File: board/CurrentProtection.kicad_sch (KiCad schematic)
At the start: 0 parts

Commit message: Schematics without values
Votlage Sensing circuit schematic
Oring controller circuit schematic
No values for components yet
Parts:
- added BT1, BT2: Battery, symbol Device:Battery
- added C1, C2, C3, C4, C5: C, symbol Device:C
- added D1, D2, D3, D4, D5: SS16, Diode_SMD:D_SMA, symbol Diode:SS16
- added D6: LED, symbol Device:LED
- added Q1, Q2, Q3: DMN3008SFG, Package_SON:Diodes_PowerDI3333-8, symbol Transistor_FET:DMN3008SFG
- added R1, R2, R27: R_US, symbol Device:R_US
- added U1, U2, U3: LM5050MK-1_NOPB, LM5050MK-1_NOPB:SOT95P280X110-6N, symbol LM5050MK-1_NOPB:LM5050MK-1_NOPB
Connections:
- new net: BT2.1 (+), D5.1 (K), Q3.1 (S), Q3.2 (S), Q3.3 (S), U3.4 (IN)
- new net: C2.1, R1.2, U1.1 (VS)
- new net: Q1.4 (G), U1.5 (GATE)
- new net: D6.2 (A), R27.2
- new net: BT1.1 (+), D4.1 (K), Q2.1 (S), Q2.2 (S), Q2.3 (S), U2.4 (IN)
- new net: Q2.4 (G), U2.5 (GATE)
- new net: Q3.4 (G), U3.5 (GATE)
- new net: D1.2 (A), D2.2 (A)
- new net +24V: C1.1, D1.1 (K), Q1.1 (S), Q1.2 (S), Q1.3 (S), U1.4 (IN)
- new net GND: BT1.2 (-), BT2.2 (-), C1.2, C2.2, C3.2, C4.2, C5.2, D2.1 (K), D3.2 (A), D4.2 (A), D5.2 (A), D6.1 (K), R2.2, U1.2 (GND), U1.3 (OFF), U2.2 (GND), U3.2 (GND)
- new net Vout: C3.1, C4.1, C5.1, D3.1 (K), Q1.5 (D), Q2.5 (D), Q3.5 (D), R1.1, R2.1, U1.6 (OUT), U2.1 (VS), U2.6 (OUT), U3.1 (VS), U3.6 (OUT)
- new net VoutPin: R27.1
- no-connect marks 0 -> 2
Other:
- note added: "LED CIRCUITS"

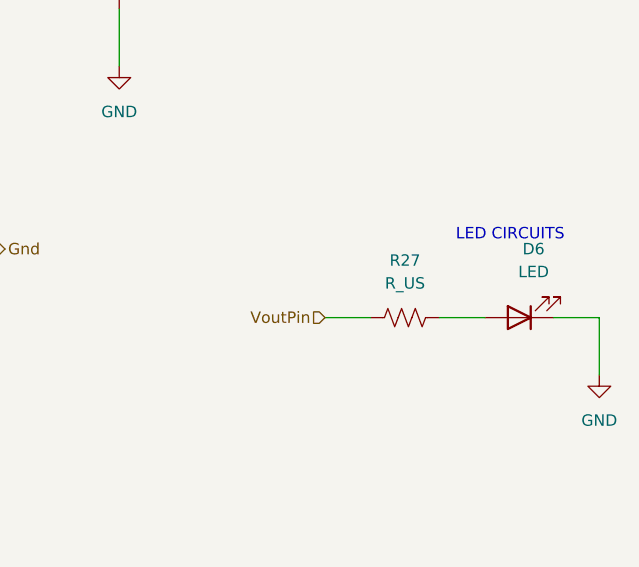
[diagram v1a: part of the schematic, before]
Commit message: Resistor Values
Added resistor values for everything on voltage sensing circuit
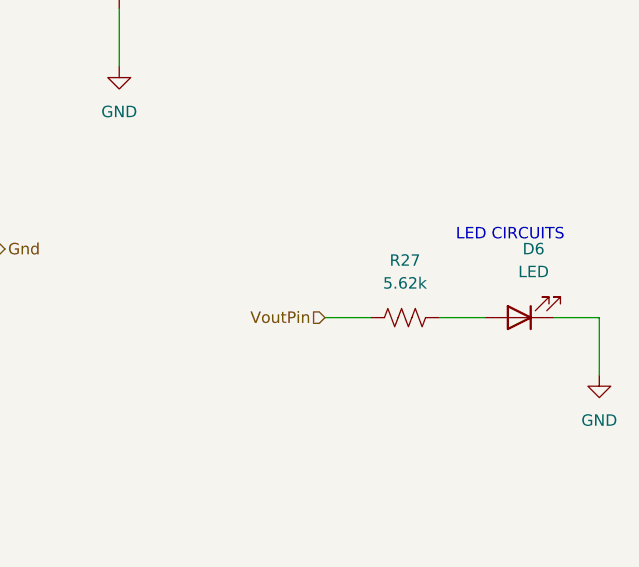
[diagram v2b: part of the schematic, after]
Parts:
- R27: value R_US -> 5.62k
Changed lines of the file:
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@@
 			)
 		)
-		(property "Value" "R_US"
+		(property "Value" "5.62k"
 			(at 176.53 138.43 90)
 			(effects

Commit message: Changed Flags
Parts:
- removed C1, C2, C3: C, symbol Device:C
- removed D1, D2, D3: SS16, Diode_SMD:D_SMA, symbol Diode:SS16
- removed Q1, Q2: DMN3008SFG, Package_SON:Diodes_PowerDI3333-8, symbol Transistor_FET:DMN3008SFG
- removed R1: R_US, symbol Device:R_US
- removed U1: LM5050MK-1_NOPB, LM5050MK-1_NOPB:SOT95P280X110-6N, symbol LM5050MK-1_NOPB:LM5050MK-1_NOPB
- added Q4: IPB180N10S4-02, Package_TO_SOT_SMD:TO-263-6, symbol Transistor_FET:IPB180N10S4-02
- BT1: footprint (none) -> MRDT_Connectors:Square_Anderson_2_H_Side_By_Side_PV
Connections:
- net VoutPin is gone; now on net +24V: R27.1
- net Vout: now also Q4.2 (S), Q4.3 (S), Q4.5 (S), Q4.6 (S), Q4.7 (S)
- net at BT1.1 (+), D4.1 (K), U2.4 (IN): now also Q4.4 (D)
- net at U2.5 (GATE): now also Q4.1 (G)

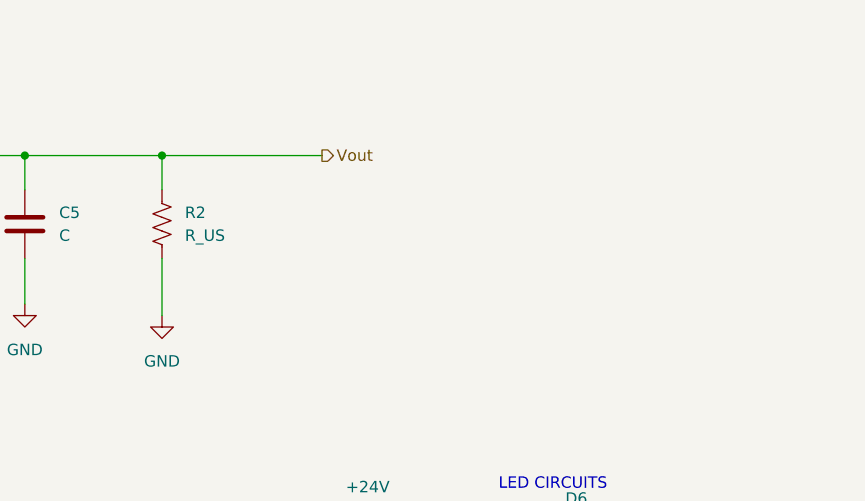
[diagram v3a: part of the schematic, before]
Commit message: Current Sensor in Current Protection
amogus
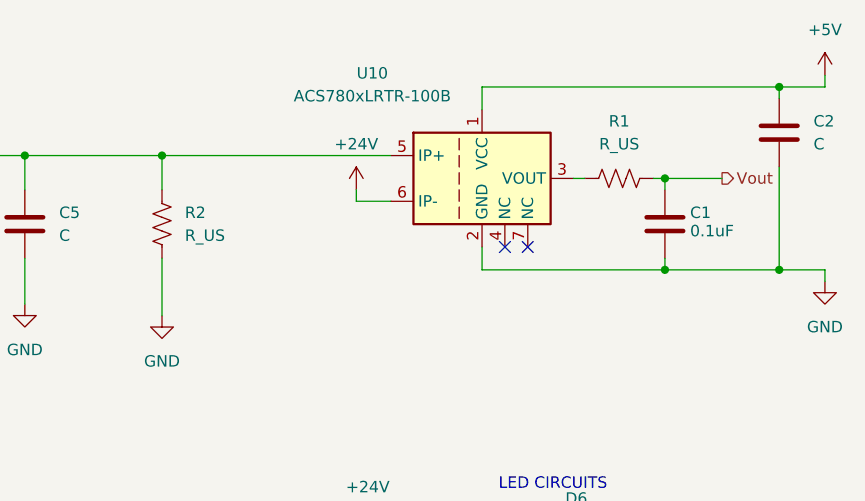
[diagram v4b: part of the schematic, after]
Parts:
- added C1: 0.1uF, symbol Device:C
- added C2: C, symbol Device:C
- added R1: R_US, symbol Device:R_US
- added U10: ACS780xLRTR-100B, Sensor_Current:Allegro_PSOF-7_4.8x6.4mm_P1.60mm, symbol Sensor_Current:ACS780xLRTR-100B
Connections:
- net +24V: now also U10.6 (IP-)
- net GND: now also C1.1, C2.2, U10.2 (GND)
- net Vout: now also C1.2, R1.2; no longer C4.1, C5.1, Q3.5 (D), Q4.2 (S), Q4.3 (S), Q4.5 (S), Q4.6 (S), Q4.7 (S), R2.1, U2.1 (VS), U2.6 (OUT), U3.1 (VS), U3.6 (OUT)
- new net: C4.1, C5.1, Q3.5 (D), Q4.2 (S), Q4.3 (S), Q4.5 (S), Q4.6 (S), Q4.7 (S), R2.1, U10.5 (IP+), U2.1 (VS), U2.6 (OUT), U3.1 (VS), U3.6 (OUT)
- new net: R1.1, U10.3 (VOUT)
- new net +5V: C2.1, U10.1 (VCC)
- no-connect marks 2 -> 4

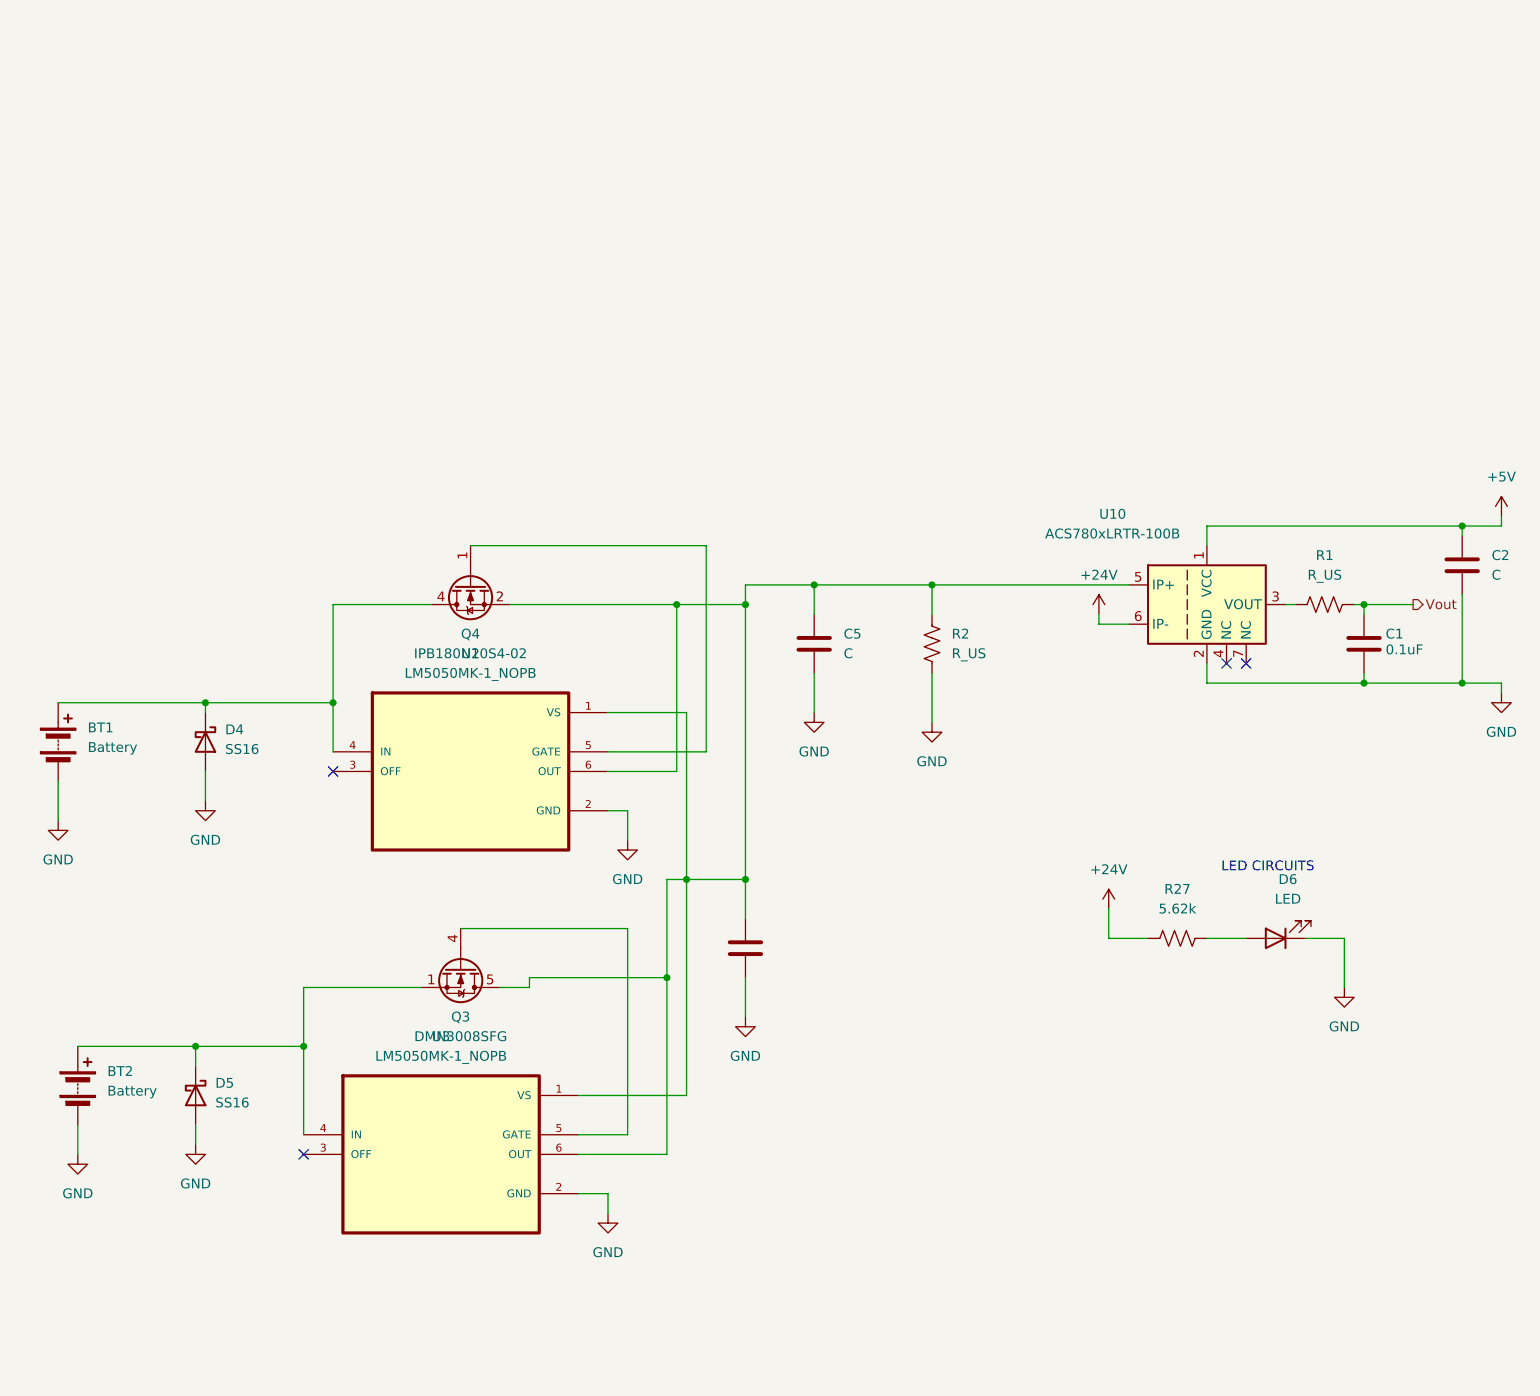
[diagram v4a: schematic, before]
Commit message: added port in voltage sensing
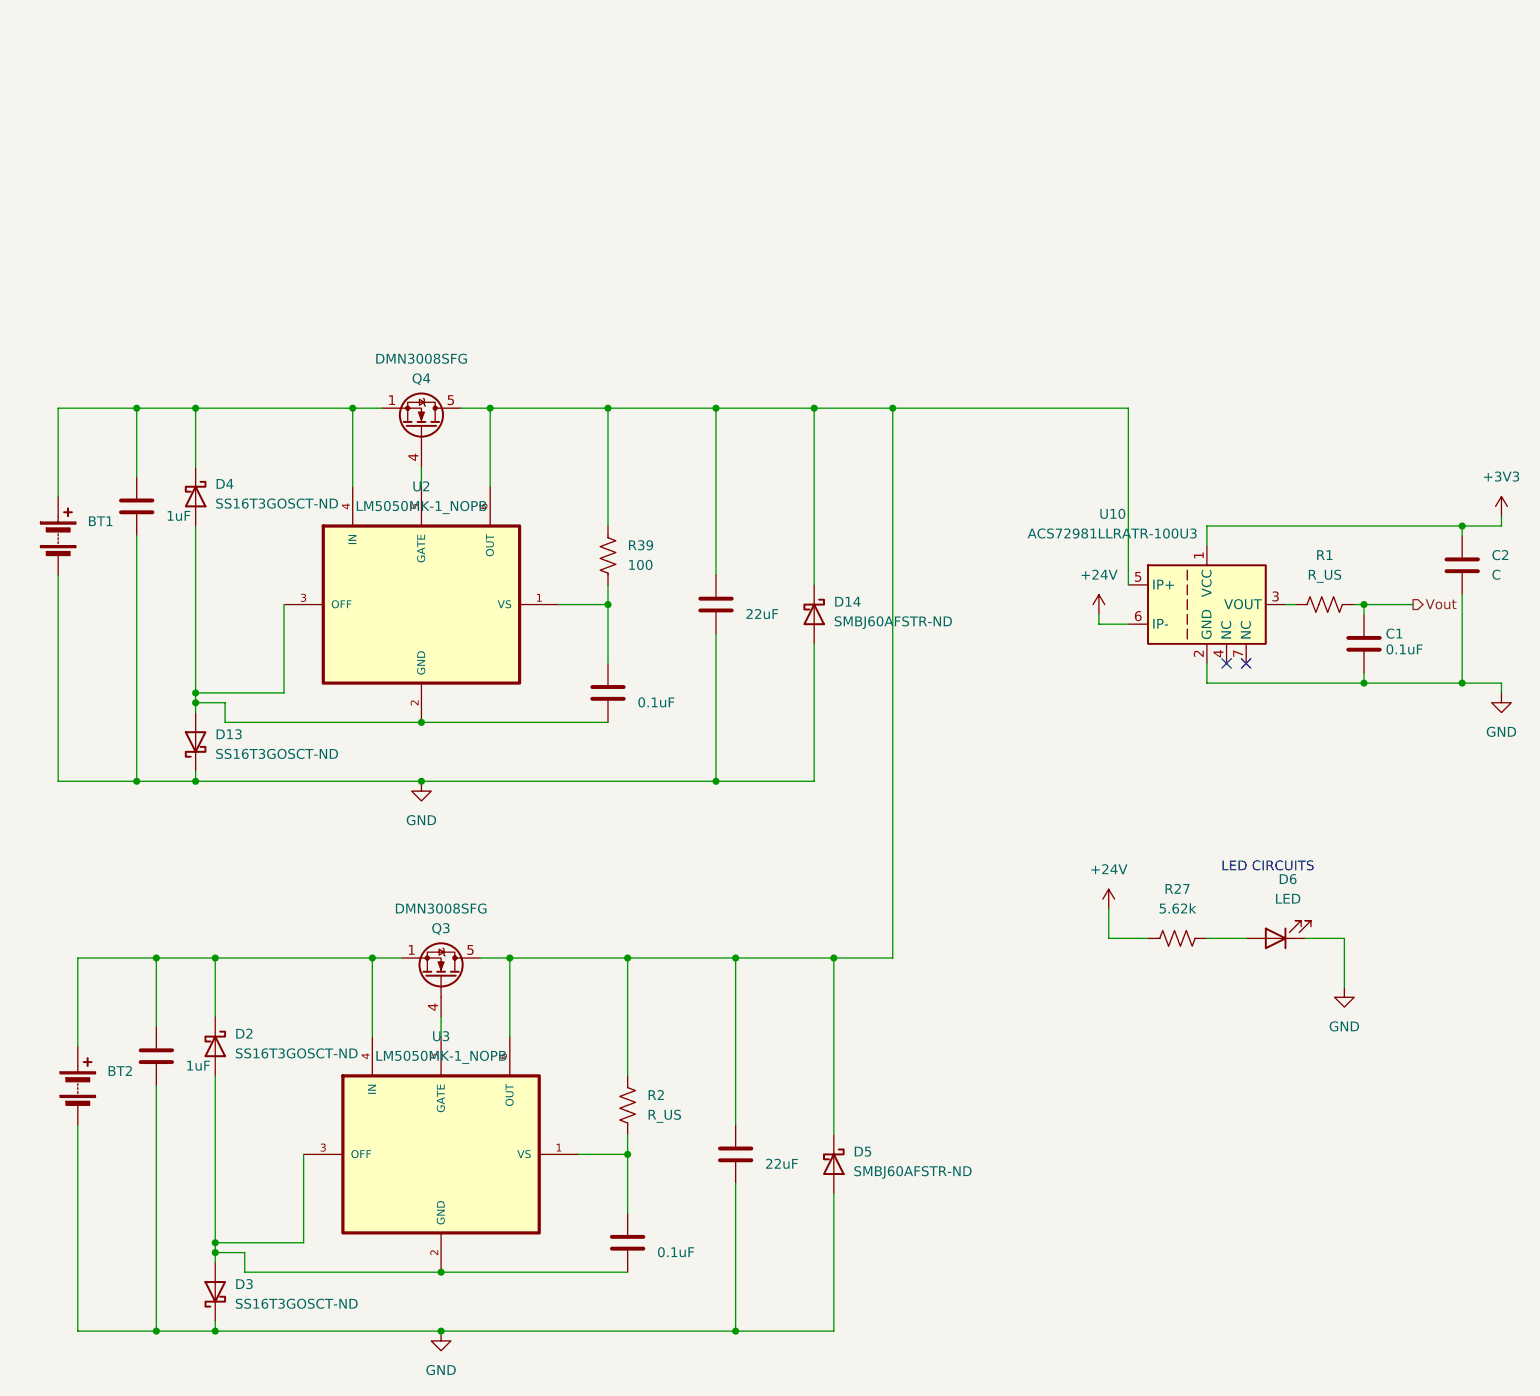
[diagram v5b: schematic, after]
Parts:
- removed Q4: IPB180N10S4-02, Package_TO_SOT_SMD:TO-263-6, symbol Transistor_FET:IPB180N10S4-02
- added C10, C12: 0.1uF, symbol Device:C
- added C11: 1uF, symbol Device:C
- added C13: 22uF, symbol Device:C
- added D13, D2, D3: SS16T3GOSCT-ND, Diode_SMD:D_SMA, symbol Diode:SS16
- added D14: SMBJ60AFSTR-ND, Diode_SMD:D_SMB, symbol Diode:SS16
- added Q4: DMN3008SFG, Package_SON:Diodes_PowerDI3333-8, symbol Transistor_FET:DMN3008SFG
- added R39: 100, symbol Device:R_US
- BT1: footprint MRDT_Connectors:Square_Anderson_2_H_Side_By_Side_PV -> (none)
- C4: value C -> 22uF
- C5: value C -> 1uF
- D4: value SS16 -> SS16T3GOSCT-ND
- D5: value SS16 -> SMBJ60AFSTR-ND; footprint Diode_SMD:D_SMA -> Diode_SMD:D_SMB
- U10: value ACS780xLRTR-100B -> ACS72981LLRATR-100U3
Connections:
- net GND: now also C11.2, C13.2, D13.1 (K), D14.2 (A), D3.1 (K); no longer D4.2 (A), R2.2, U2.2 (GND), U3.2 (GND)
- net at BT2.1 (+), Q3.1 (S), Q3.2 (S)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: now also C5.1, D2.1 (K); no longer D5.1 (K)
- net at U2.5 (GATE): now also Q4.4 (G)
- net at C4.1, Q3.5 (D), U10.5 (IP+)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: now also D5.1 (K), R2.2, C13.1, D14.1 (K), Q4.5 (D), R39.2; no longer C5.1, R2.1, U2.1 (VS), U3.1 (VS)
- net at BT1.1 (+), D4.1 (K), U2.4 (IN): now also C11.1, Q4.1 (S), Q4.2 (S), Q4.3 (S)
- net at U2.3 (OFF): now also D4.2 (A), U2.2 (GND), C12.2, D13.2 (A)
- net at U3.3 (OFF): now also U3.2 (GND), C10.2, D2.2 (A), D3.2 (A)
- net +5V renamed +3V3
- new net: C12.1, R39.1, U2.1 (VS)
- new net: C10.1, R2.1, U3.1 (VS)
- no-connect marks 4 -> 2
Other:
- moved on the sheet: Q3
